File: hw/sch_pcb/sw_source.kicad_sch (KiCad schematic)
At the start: 37 parts, among them U1 TPS631000DRLR

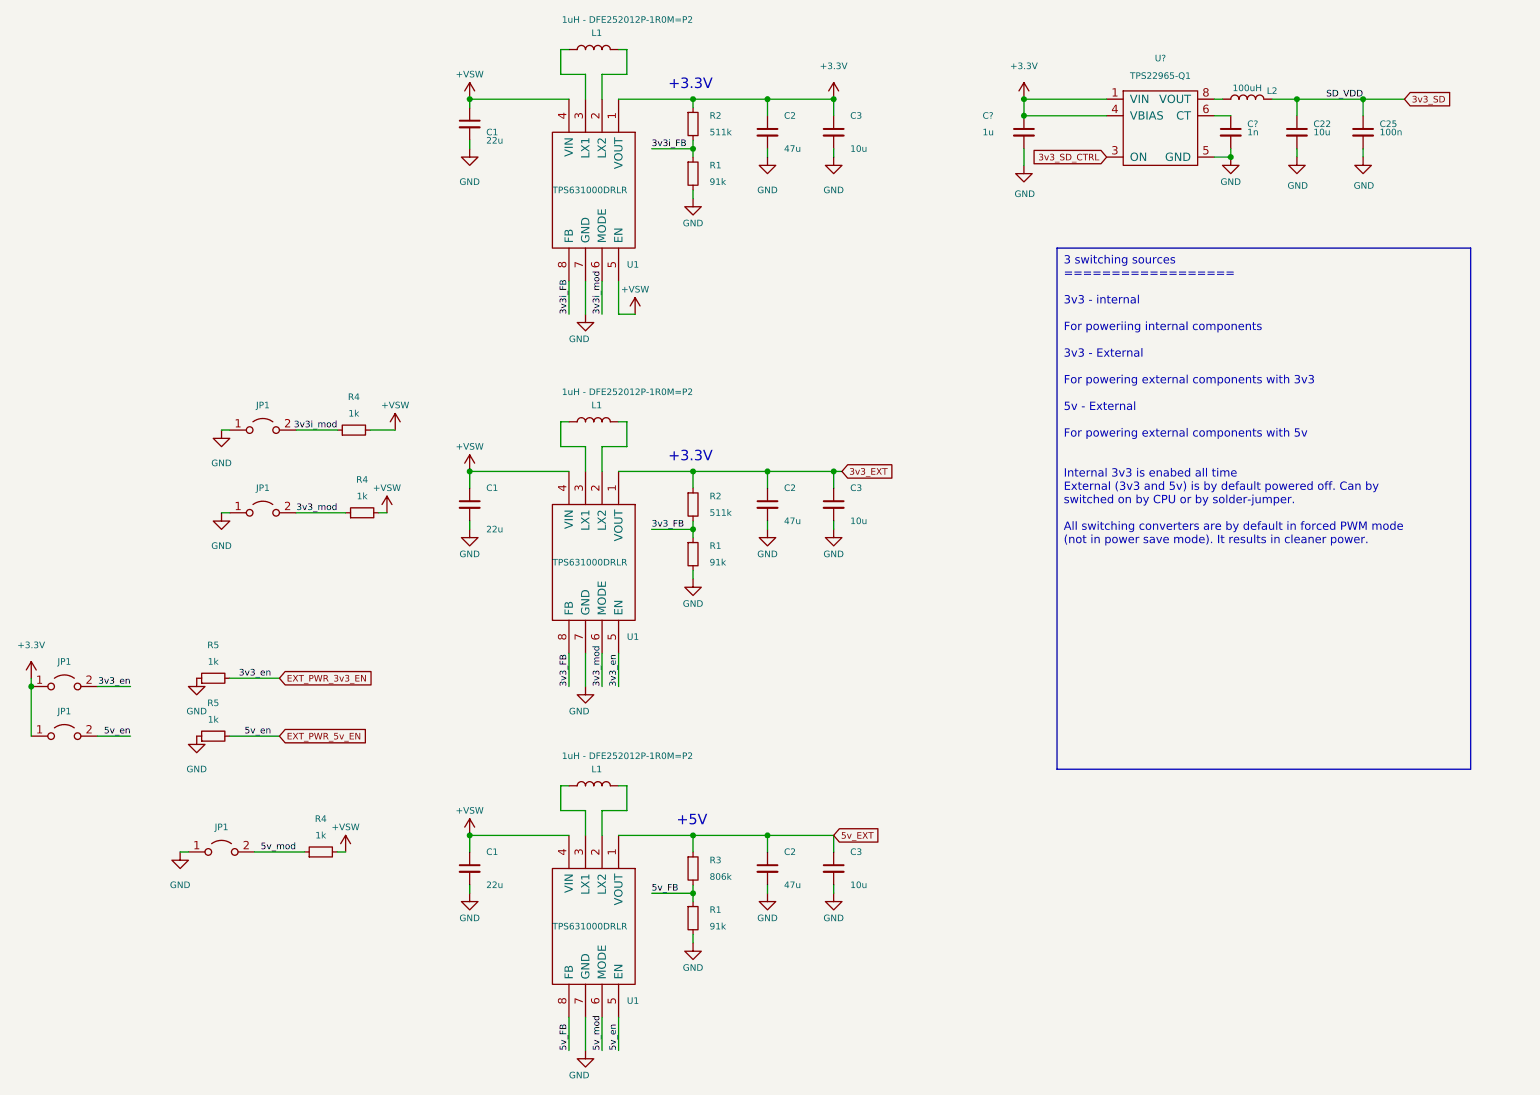
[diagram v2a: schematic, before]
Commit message: Updates in schematics, improved readability
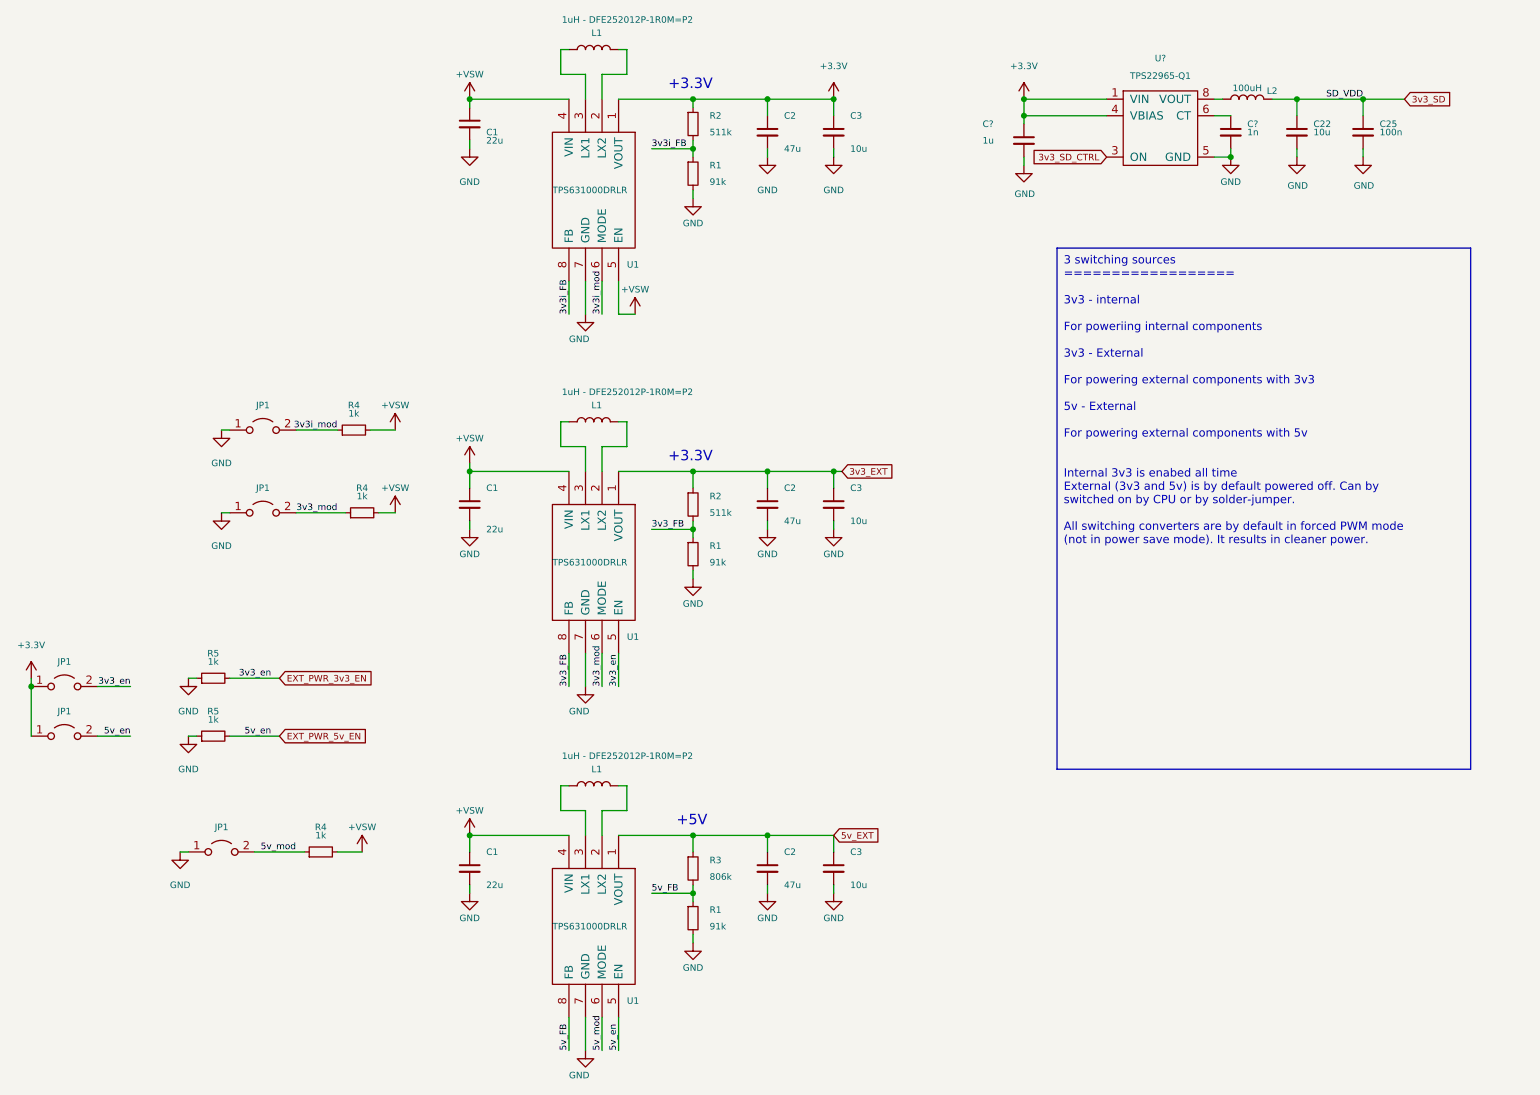
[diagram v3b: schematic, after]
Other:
- moved on the sheet: C?

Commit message: minor updates, update kibot
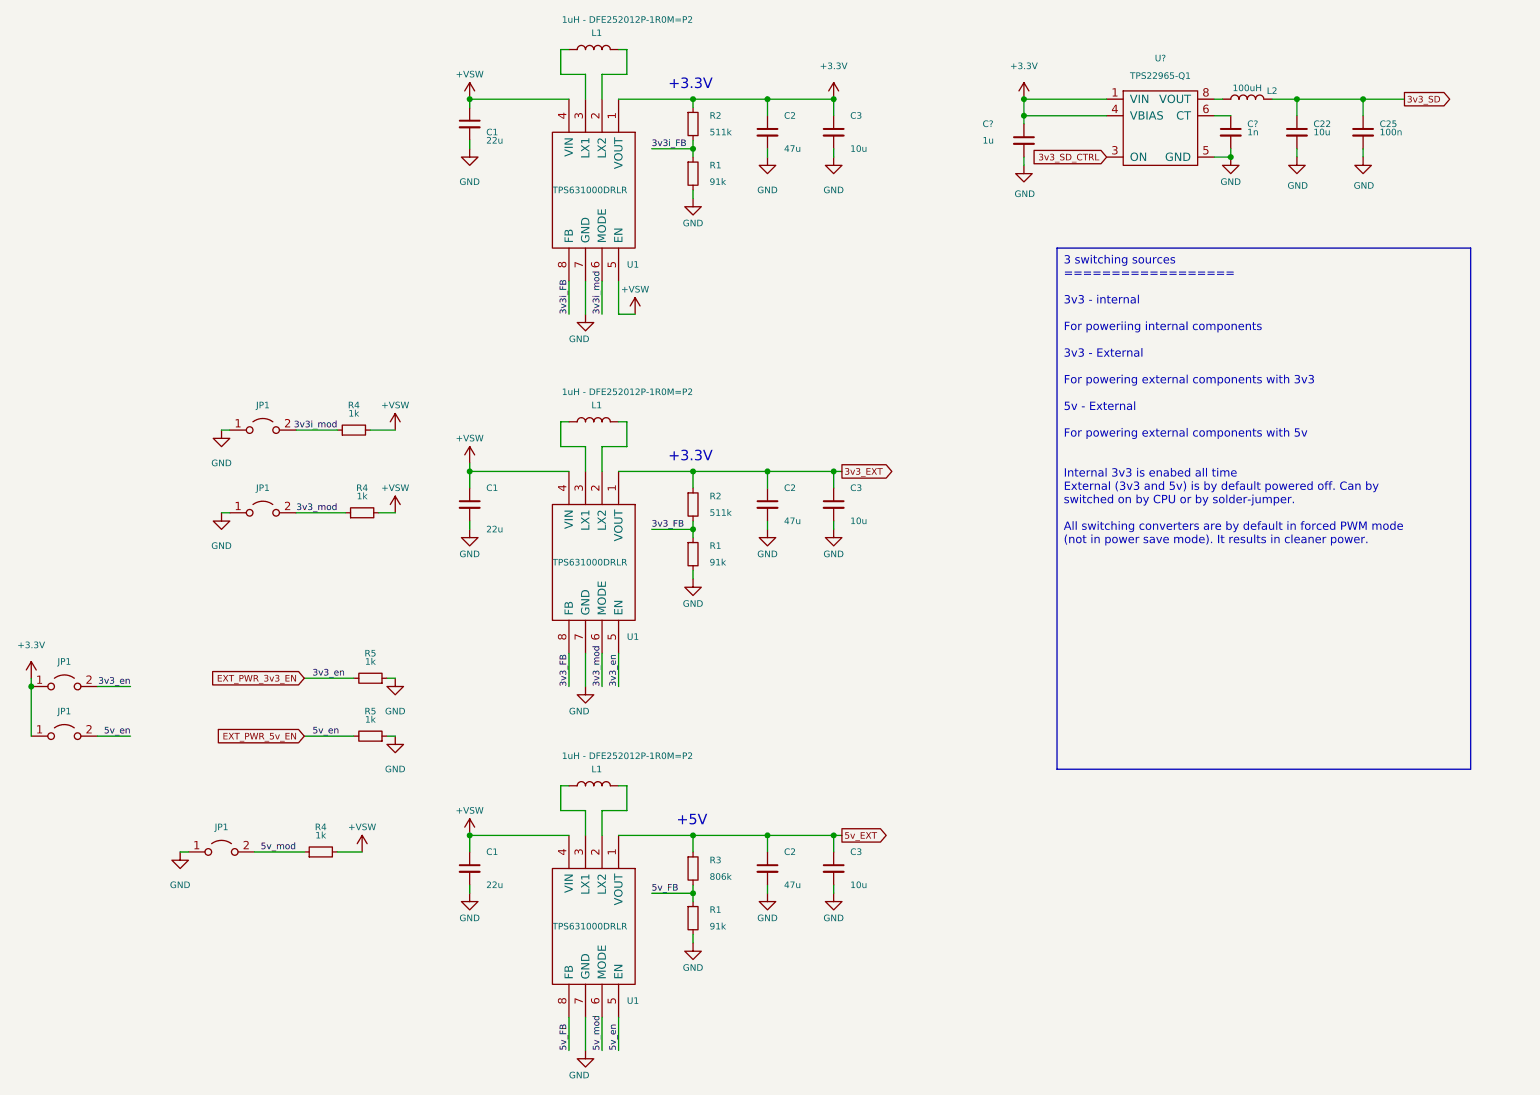
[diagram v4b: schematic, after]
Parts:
- R1: UST_ID (none) -> 5c70984712875079b91f8a95
- R2: UST_ID (none) -> 650b5a43462c6d9e7205468e
- R3: UST_ID (none) -> 650b5abb462c6d9e720546b8
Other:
- moved on the sheet: R5

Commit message: resave project
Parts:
- U?: footprint Package_SON:WSON-8-1EP_2x2mm_P0.5mm_EP0.9x1.6mm_ThermalVias -> Package_SON:WSON-8-1EP_2x2mm_P0.5mm_EP0.9x1.6mm
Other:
- moved on the sheet: C22, C25, C?, L2, U?
